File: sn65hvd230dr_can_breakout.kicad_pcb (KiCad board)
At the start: 2 copper layers, 43.1 x 18.8 mm, 12 parts, among them P1 CONN_01X02, P2 Mode, P3 CONN_01X02, U1 sn65hvd230dr

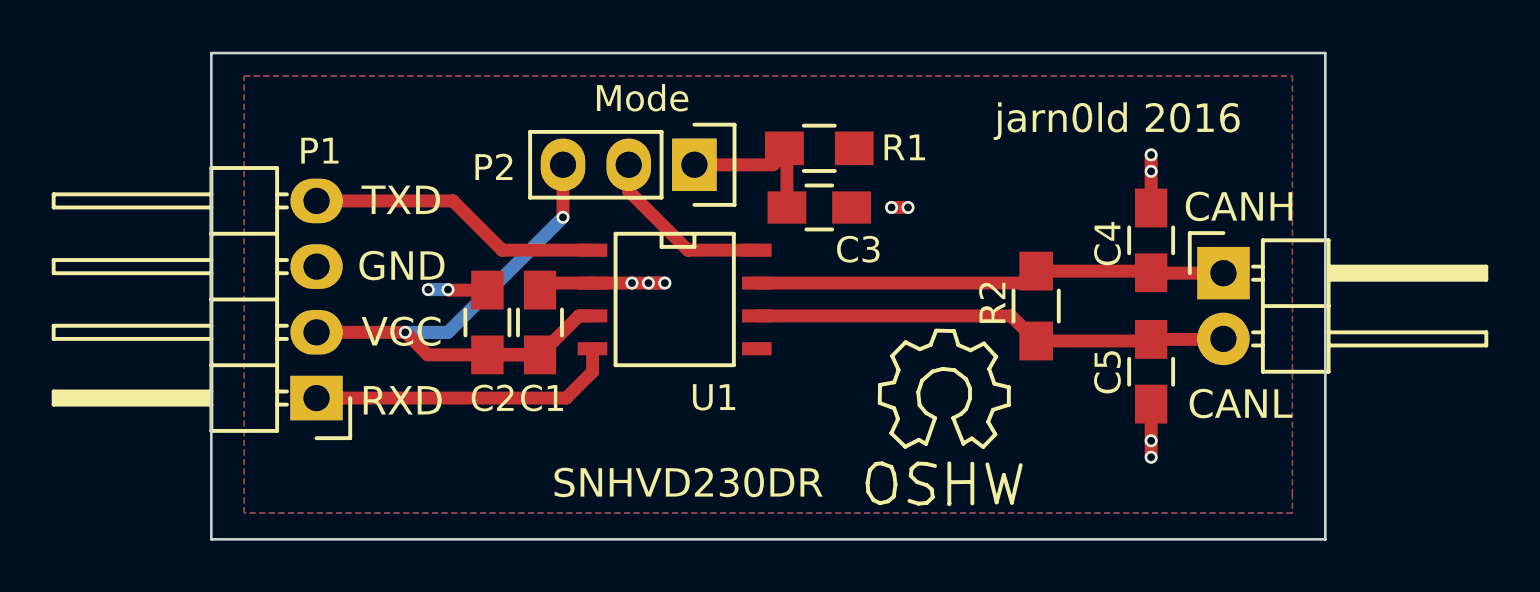
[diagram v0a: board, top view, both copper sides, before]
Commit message: set proper oshpark DRs for vias
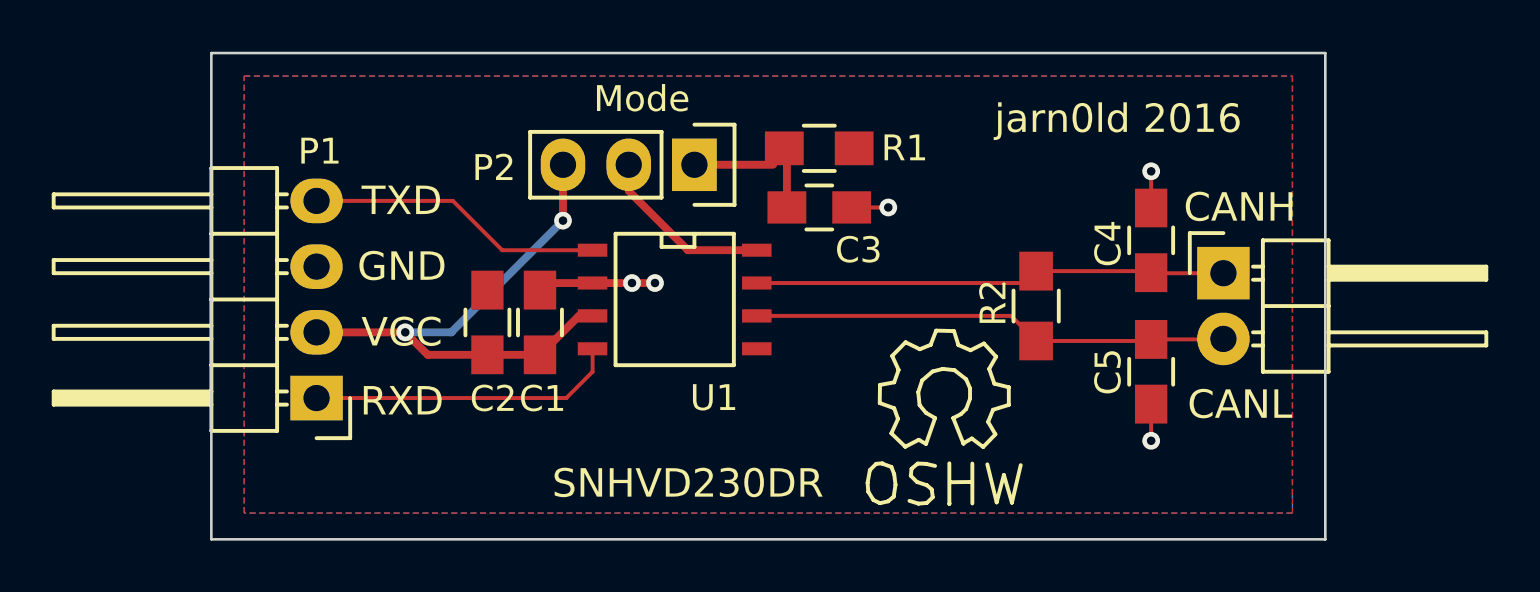
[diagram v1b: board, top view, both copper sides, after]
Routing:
- net GND: track 13.2 -> 9.32 mm, vias 11 -> 5
- net VCC: track 23.7 -> 21.7 mm
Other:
- net class Default: clearance 0.2 -> 0.1524; trace_width 0.5 -> 0.1524; via_dia 0.5 -> 0.6858; via_drill 0.3 -> 0.3302
- net class Pwr added: clearance 0.1524, trace_width 0.3048, via_dia 0.6858, via_drill 0.3302
- rule trace_clearance: 0.2 -> 0.1524
- rule trace_min: 0.18 -> 0.1524
- rule via_min_drill: 0.03302 -> 0.3302
- rule via_min_size: 0.06 -> 0.6858
